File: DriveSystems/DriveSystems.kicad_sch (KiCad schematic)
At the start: 29 parts, among them J1 Raspberry_Pi_4, M1 Motor_Servo, M2 Motor_Servo, SW1 SW_Rotary_1x2_MP, U1 RoboClaw Motor Controller, U2 5304 Gear Motor, U3 5VDC 5A UBC-C PSU, U4 24V 5V10A DCDC Stepdown, U5 RoboClaw VClamp, U6 Pwr Res

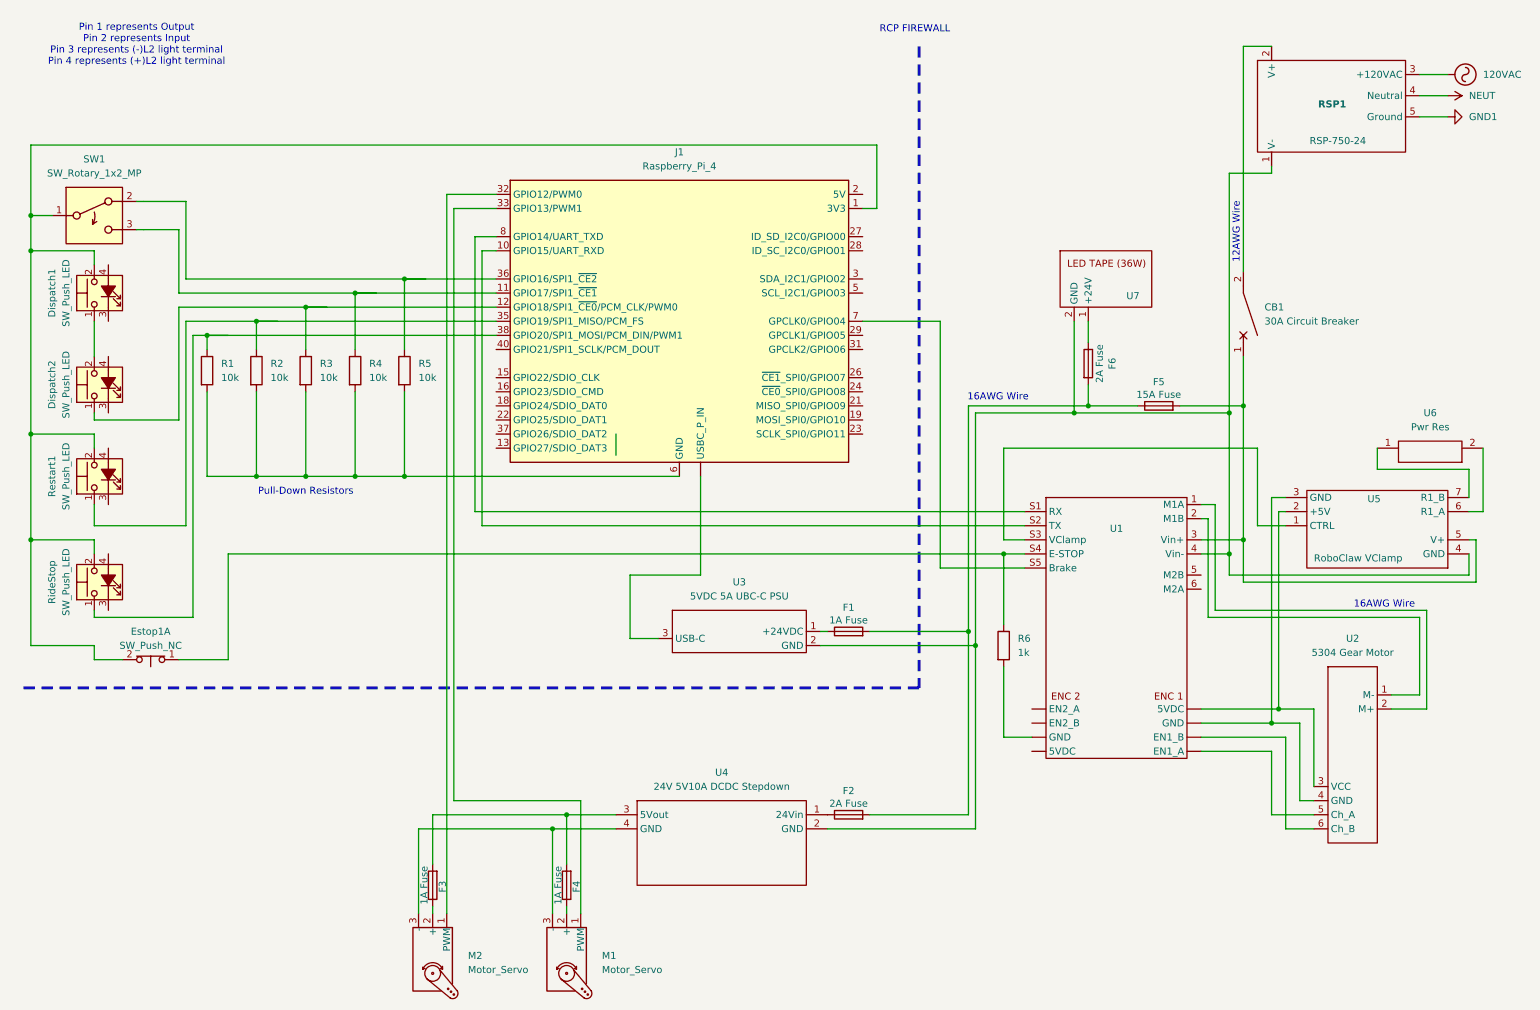
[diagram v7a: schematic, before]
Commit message: Added RJ45 connector
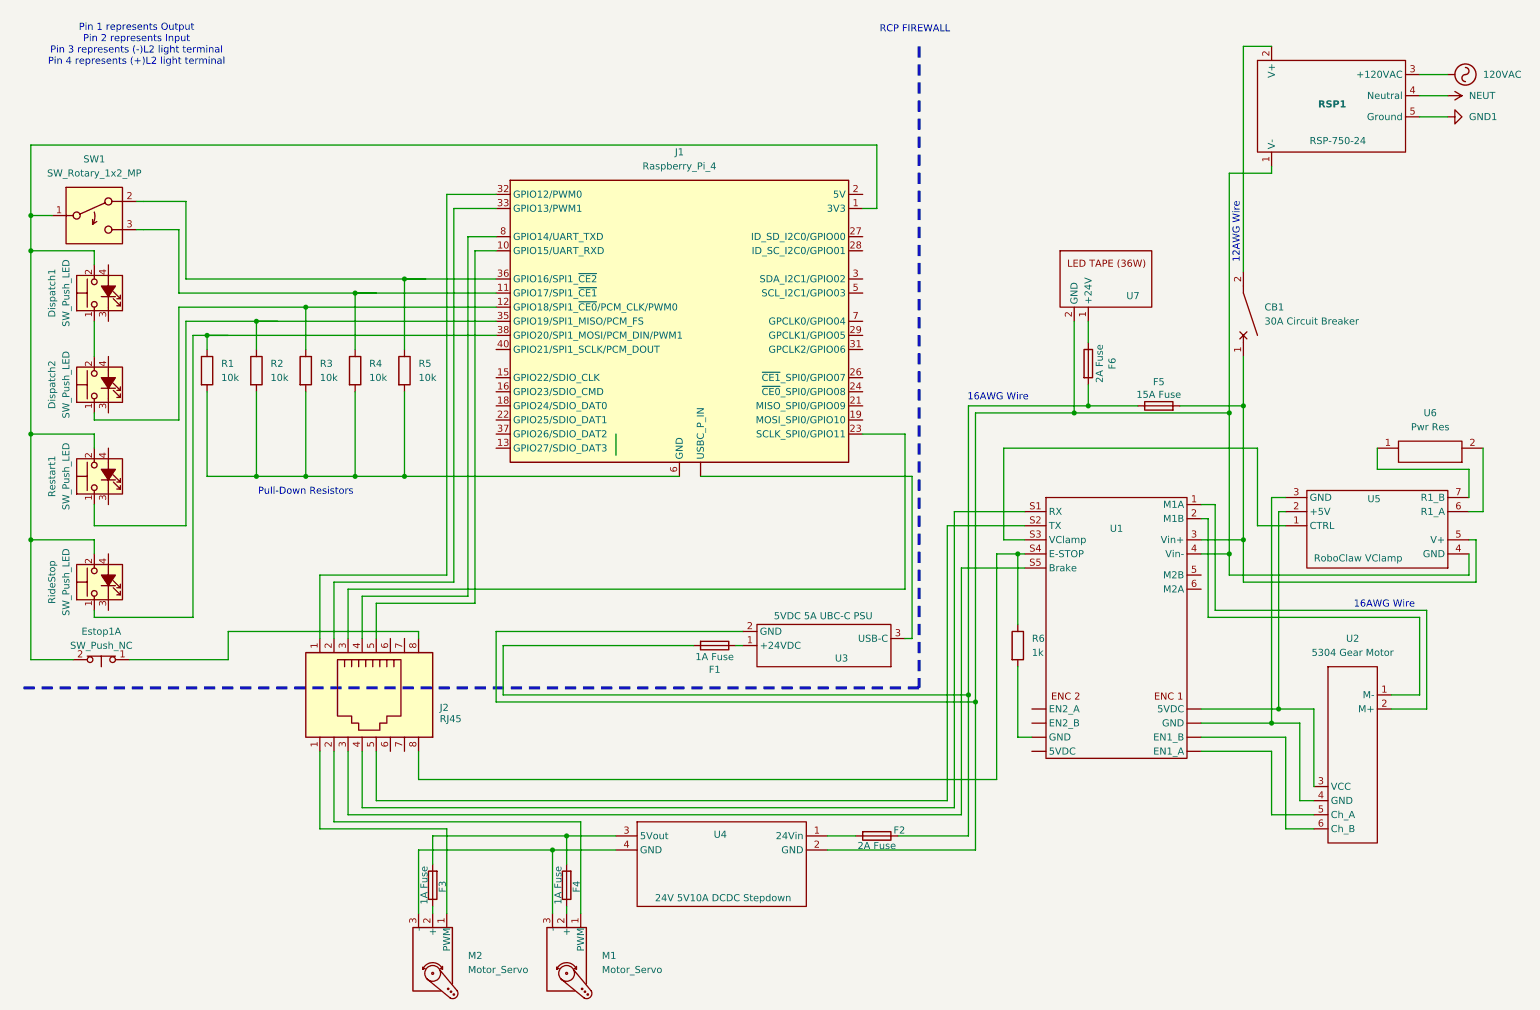
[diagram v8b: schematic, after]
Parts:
- added J2: RJ45, symbol Connector:RJ45
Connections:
- net at J1.10 (GPIO15/UART_RXD): now also J2.5; no longer U1.S2 (TX)
- net at J1.23 (SCLK_SPI0/GPIO11): now also J2.3
- net at J1.32 (GPIO12/PWM0): now also J2.1; no longer M2.1 (PWM)
- net at J1.33 (GPIO13/PWM1): now also J2.2; no longer M1.1 (PWM)
- net at J1.7 (GPCLK0/GPIO04): no longer U1.S5 (Brake)
- net at J1.8 (GPIO14/UART_TXD): now also J2.4; no longer U1.S1 (RX)
- net at U1. (EN1_A): now also R6.2
- net at R6.1, U1.S4 (E-STOP): now also J2.8; no longer Estop1.1
- net at F2.1: now also F1.2, F5.1, F6.2; no longer U4.1 (24Vin)
- new net: J2.4, U1.S1 (RX)
- new net: J2.5, U1.S2 (TX)
- new net: J2.3, U1.S5 (Brake)
- new net: F2.2, U4.1 (24Vin)
- new net: Estop1.1, J2.8
- new net: J2.1, M2.1 (PWM)
- new net: J2.2, M1.1 (PWM)
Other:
- moved on the sheet: Estop1A, F1, F2, R6, U3, U4
